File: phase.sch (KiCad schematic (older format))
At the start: 26 parts, among them U4 INA240A1PW, U5 UCC21520DW

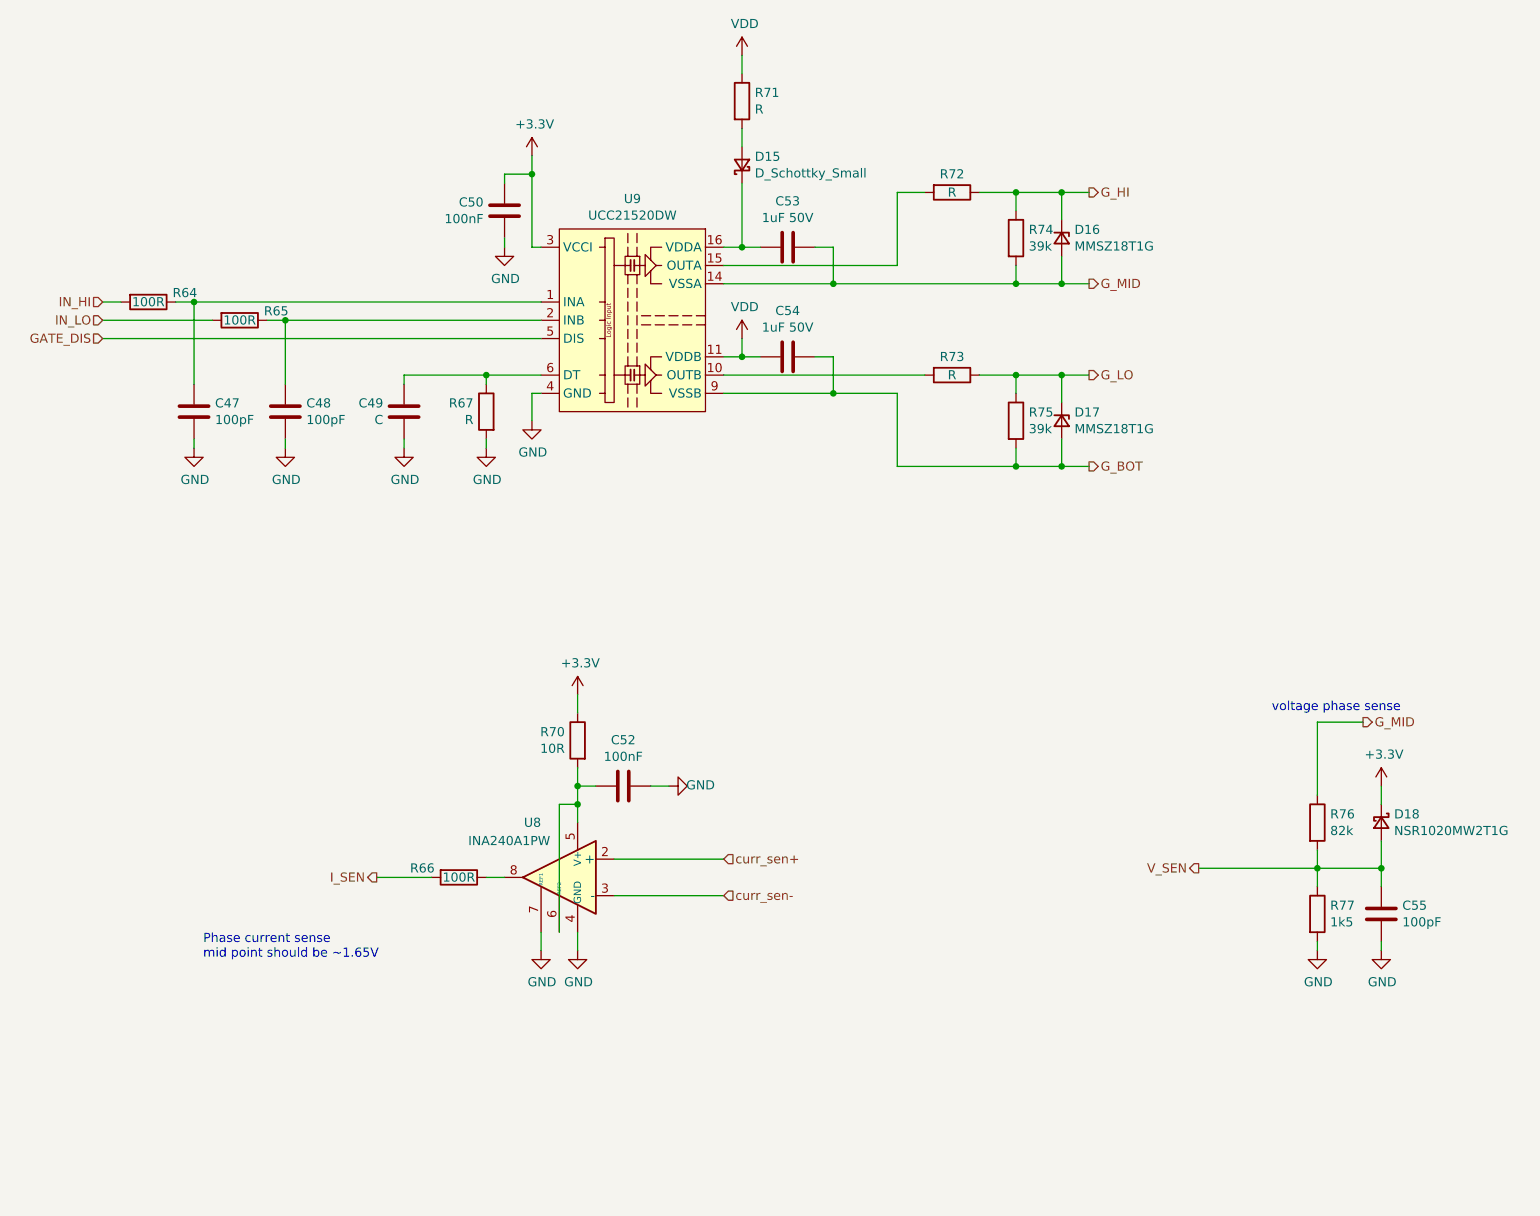
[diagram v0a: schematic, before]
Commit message: Adding LCSC part numbers
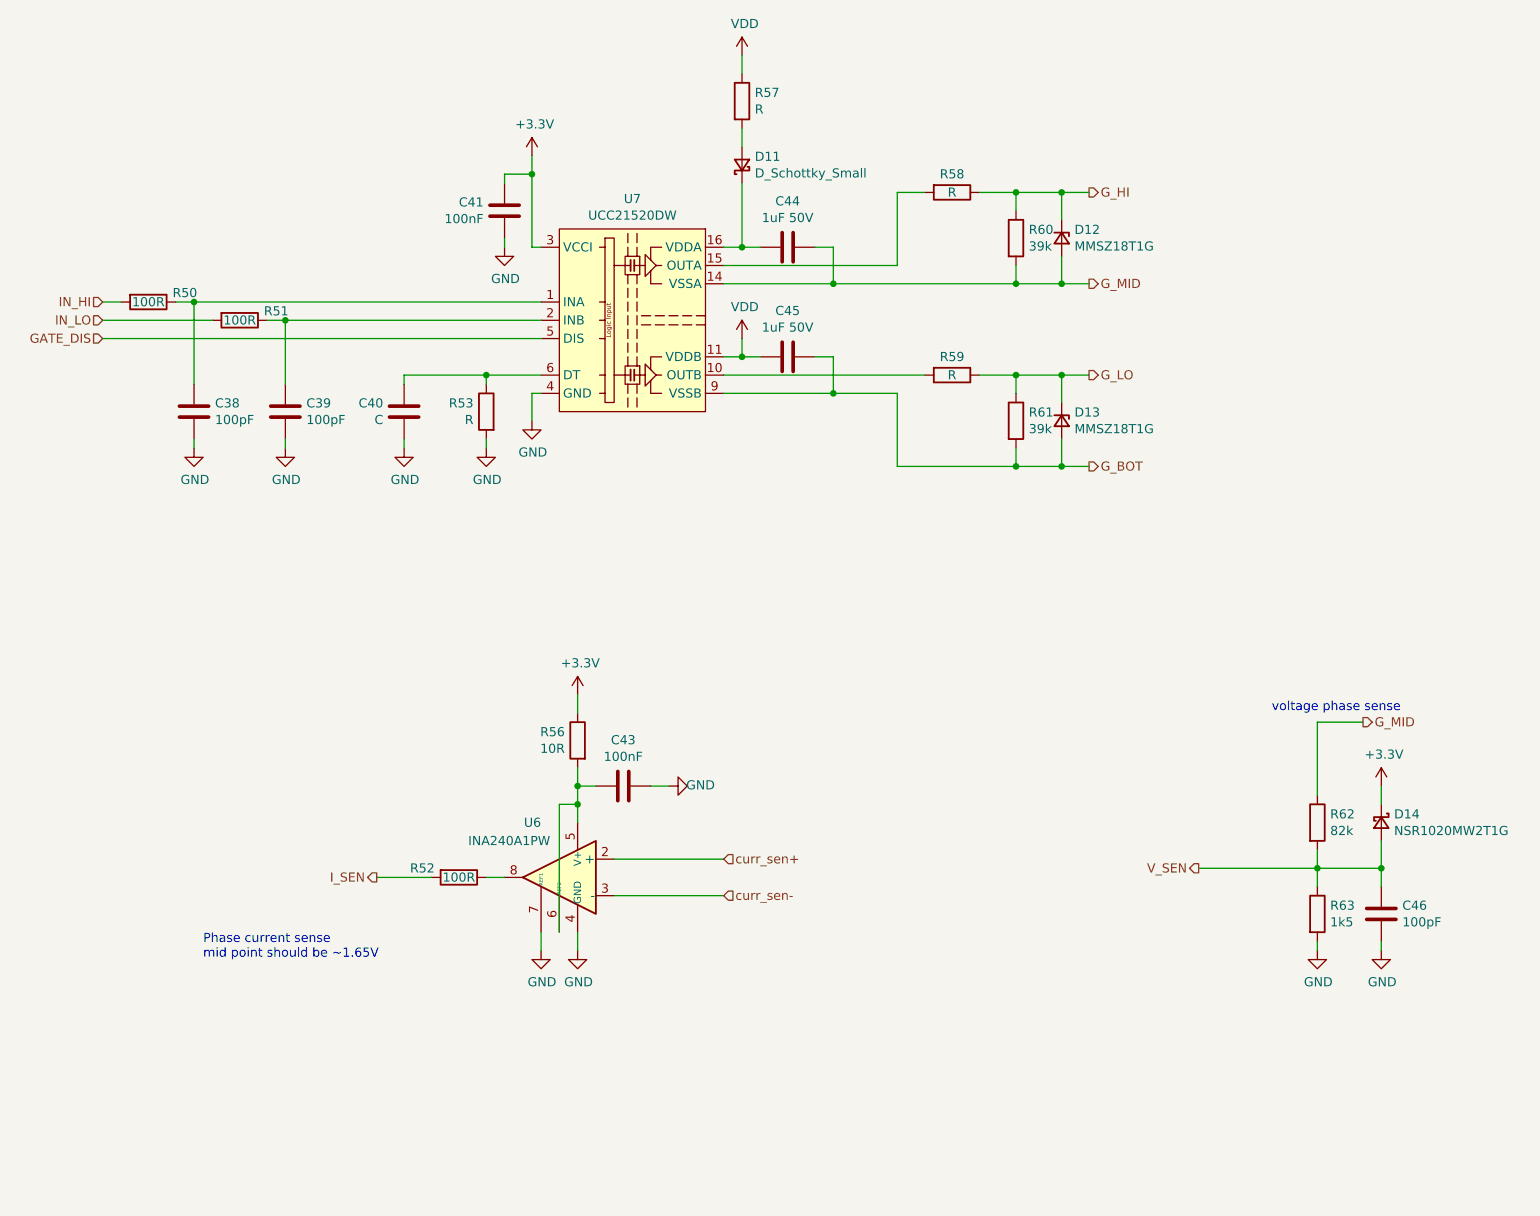
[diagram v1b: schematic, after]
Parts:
- C29, C30, C37: LCSC (none) -> C1546
- C32, C34: LCSC (none) -> C1525
- C35, C36: footprint Capacitor_SMD:C_0805_2012Metric -> Capacitor_SMD:C_0603_1608Metric; LCSC (none) -> C15849
- D8, D9: LCSC (none) -> C382948
- R36, R37, R38: LCSC (none) -> C25076
- R42: LCSC (none) -> C25077
- R46, R47: LCSC (none) -> C25783
- R48: LCSC (none) -> C4142
- R49: LCSC (none) -> C25867
- U4: LCSC (none) -> C129949
- U5: LCSC (none) -> C601651

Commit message: Twaeking the layout to fit into 100x100mm
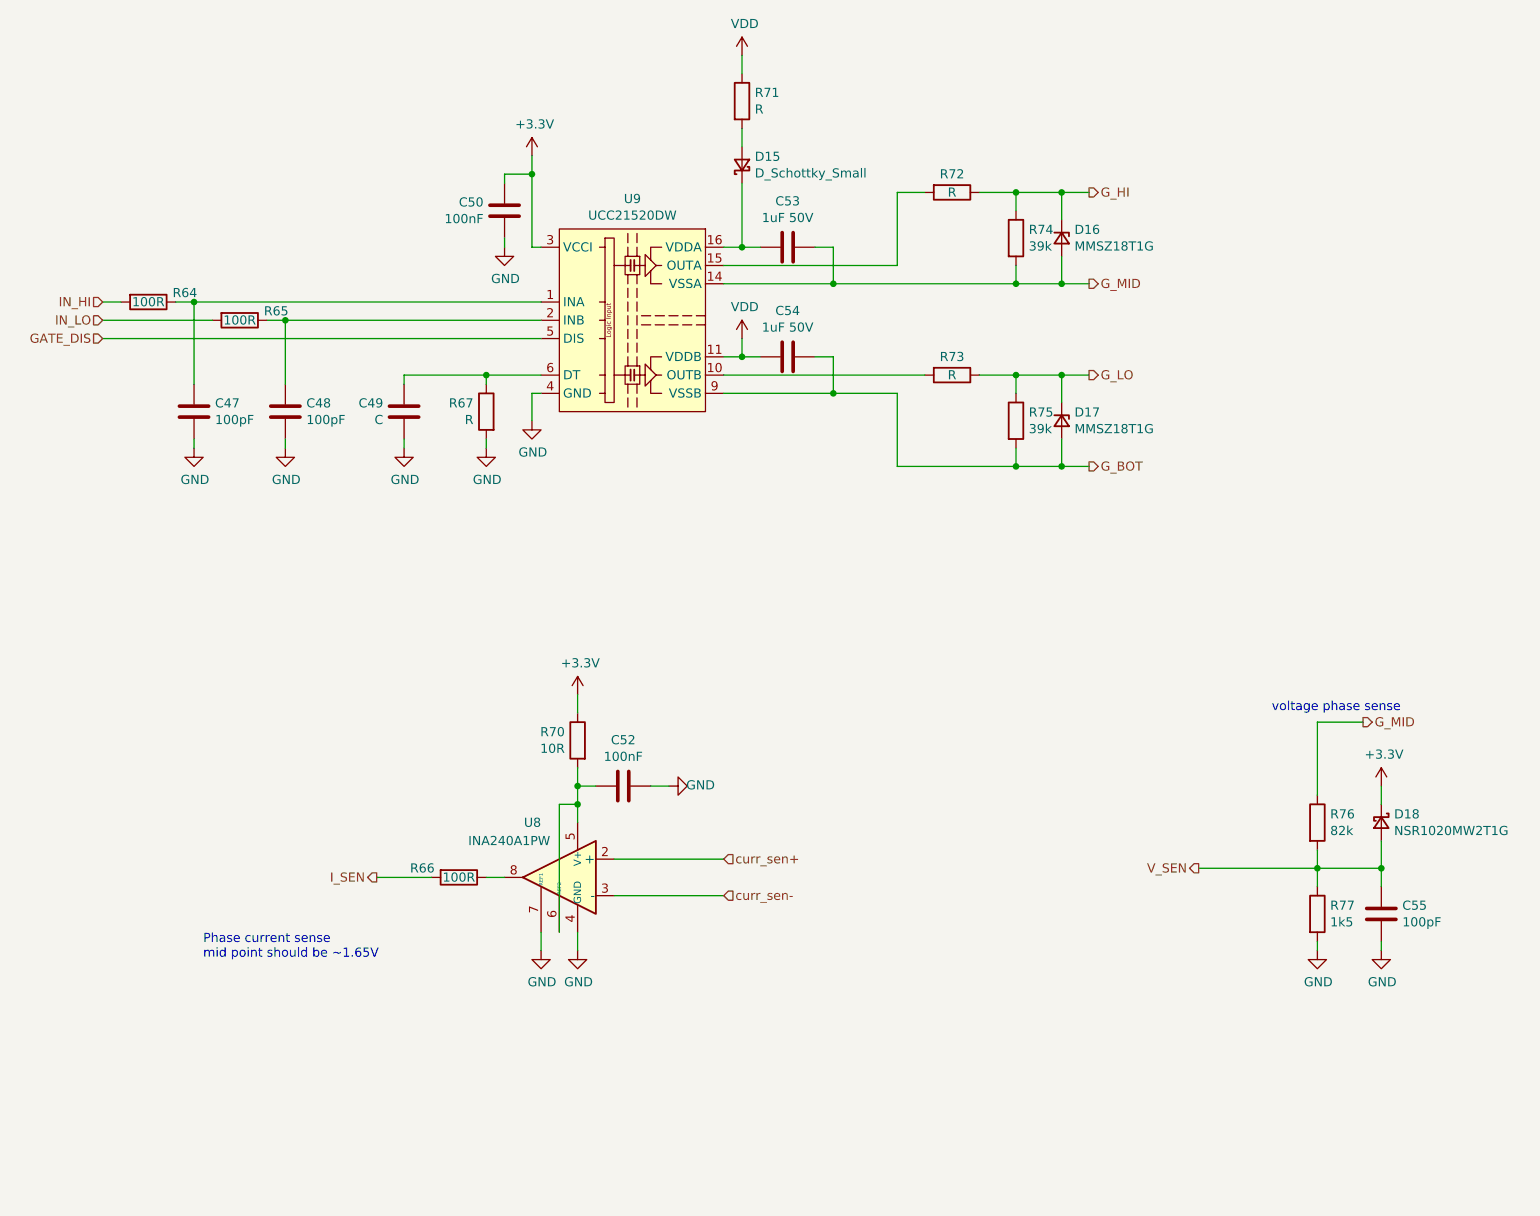
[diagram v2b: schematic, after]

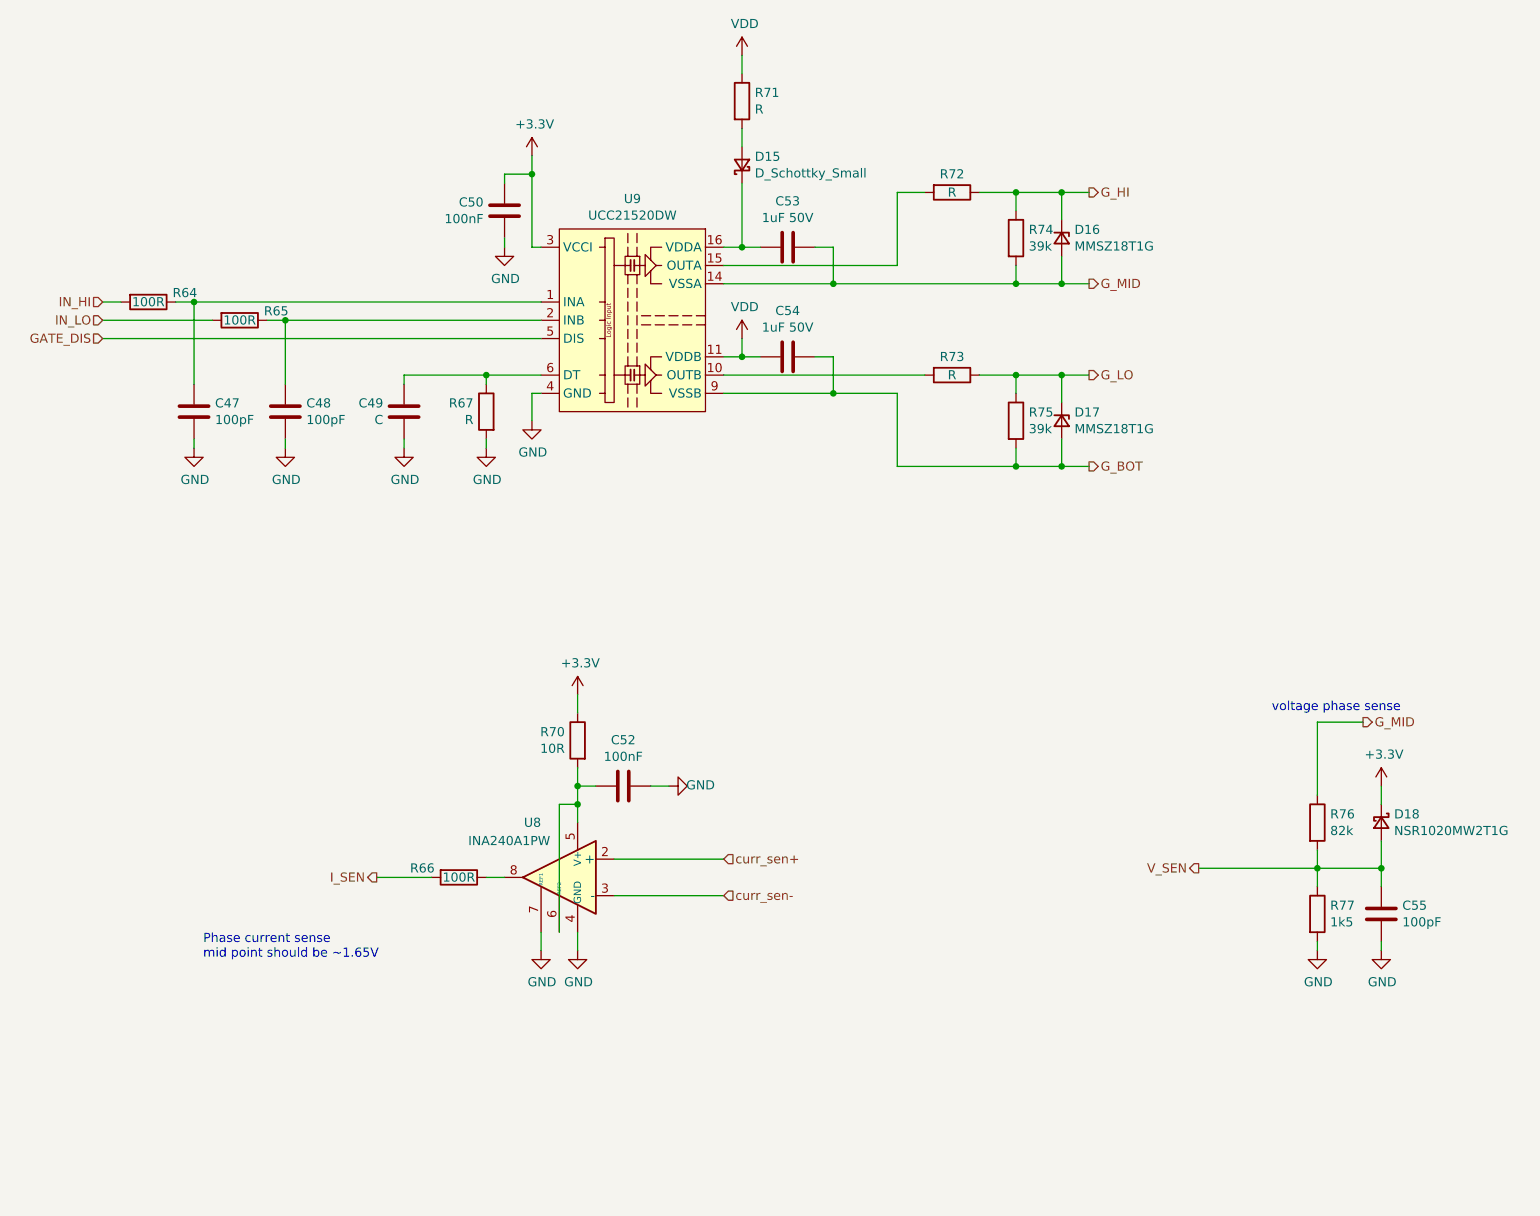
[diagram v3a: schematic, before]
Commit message: Adding some basic test tracks
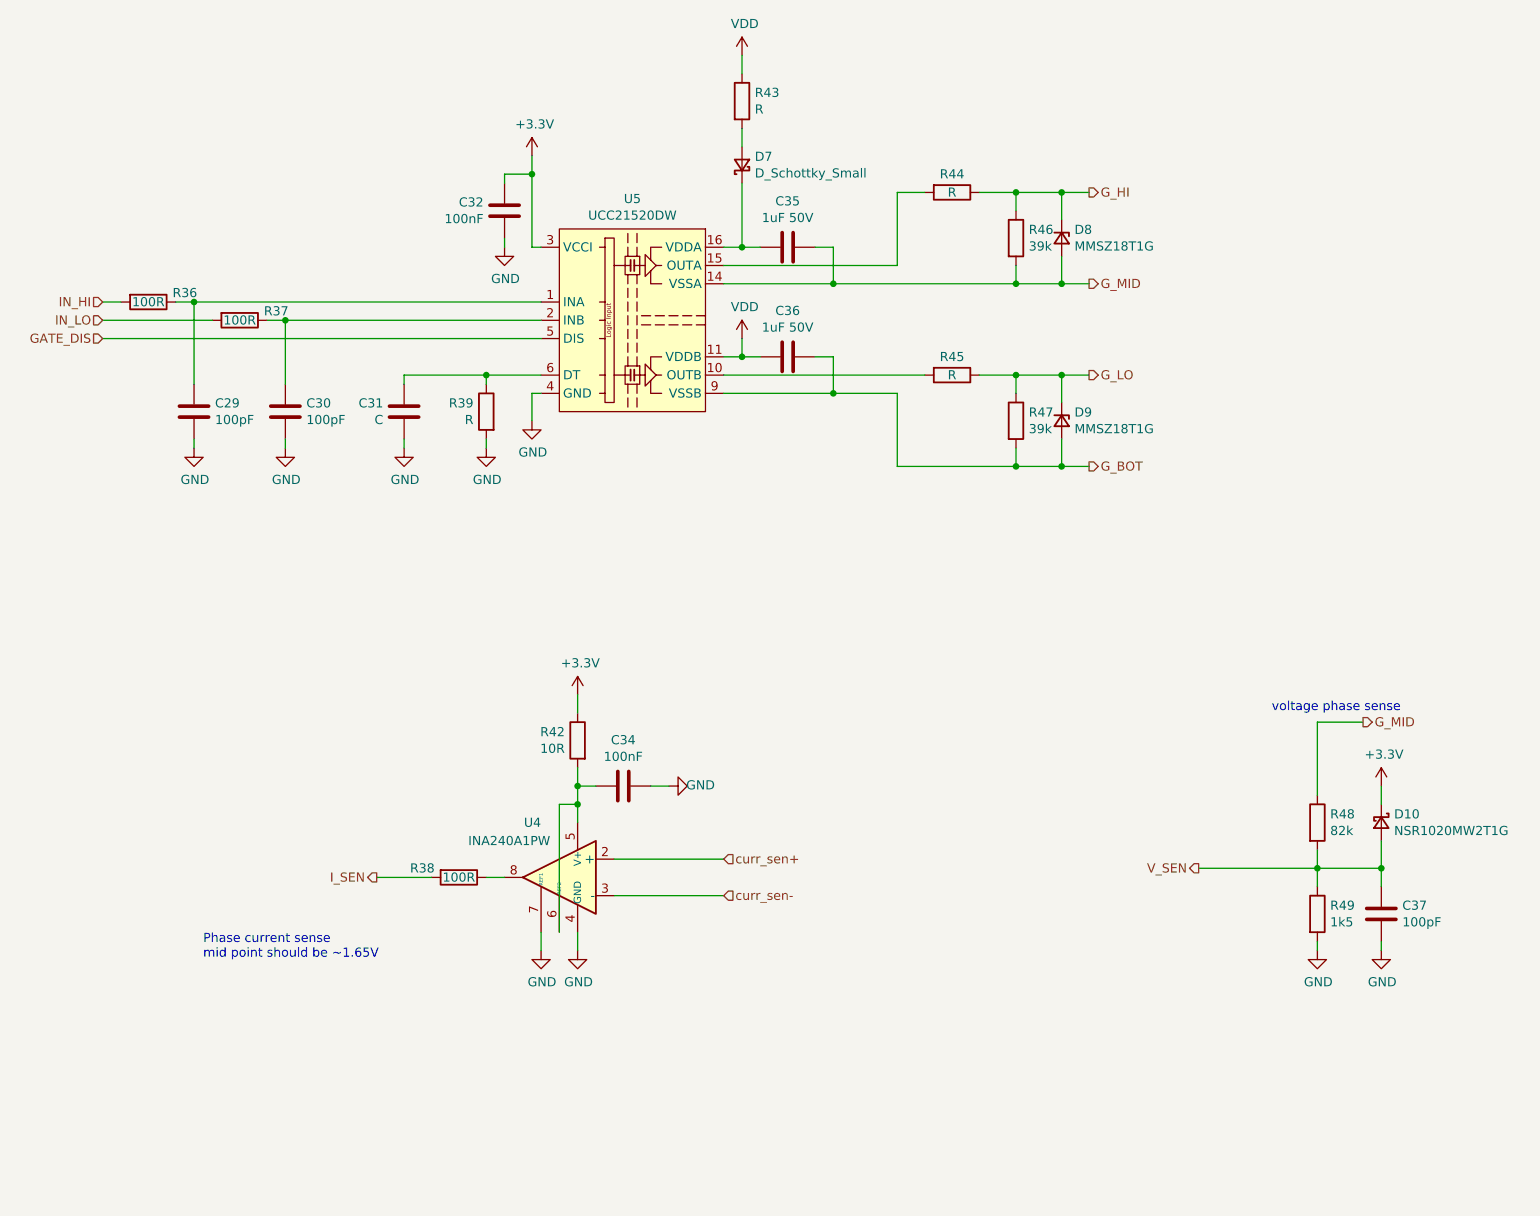
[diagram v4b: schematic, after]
